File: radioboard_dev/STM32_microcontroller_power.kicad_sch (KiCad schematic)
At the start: 27 parts

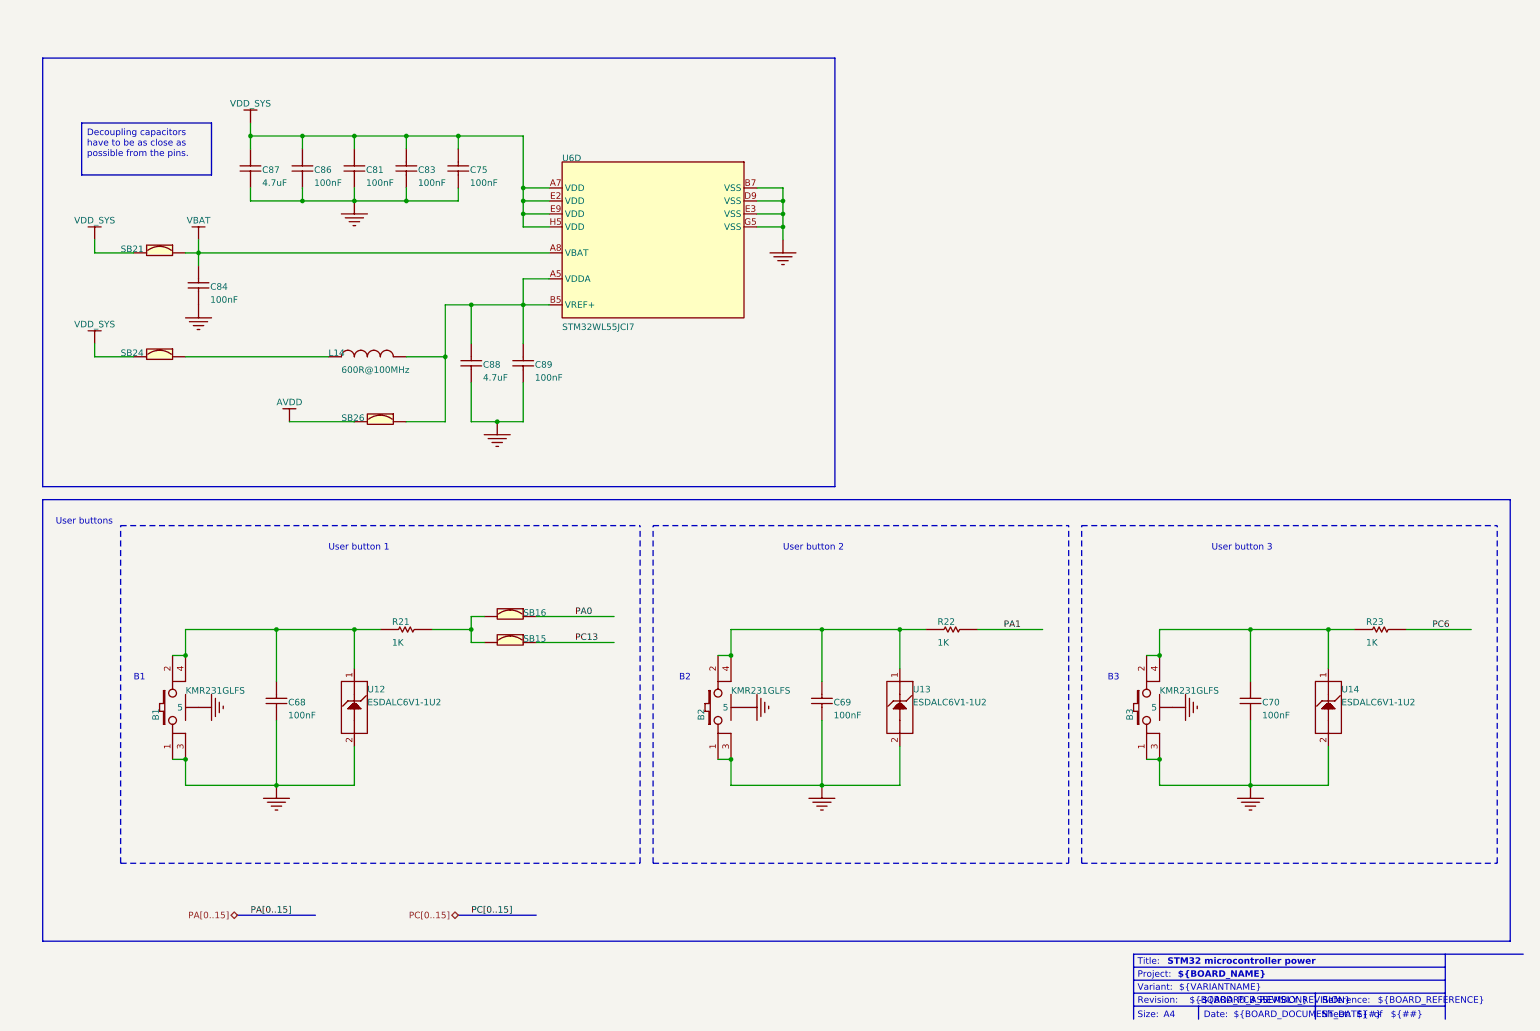
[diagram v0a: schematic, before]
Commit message: added components
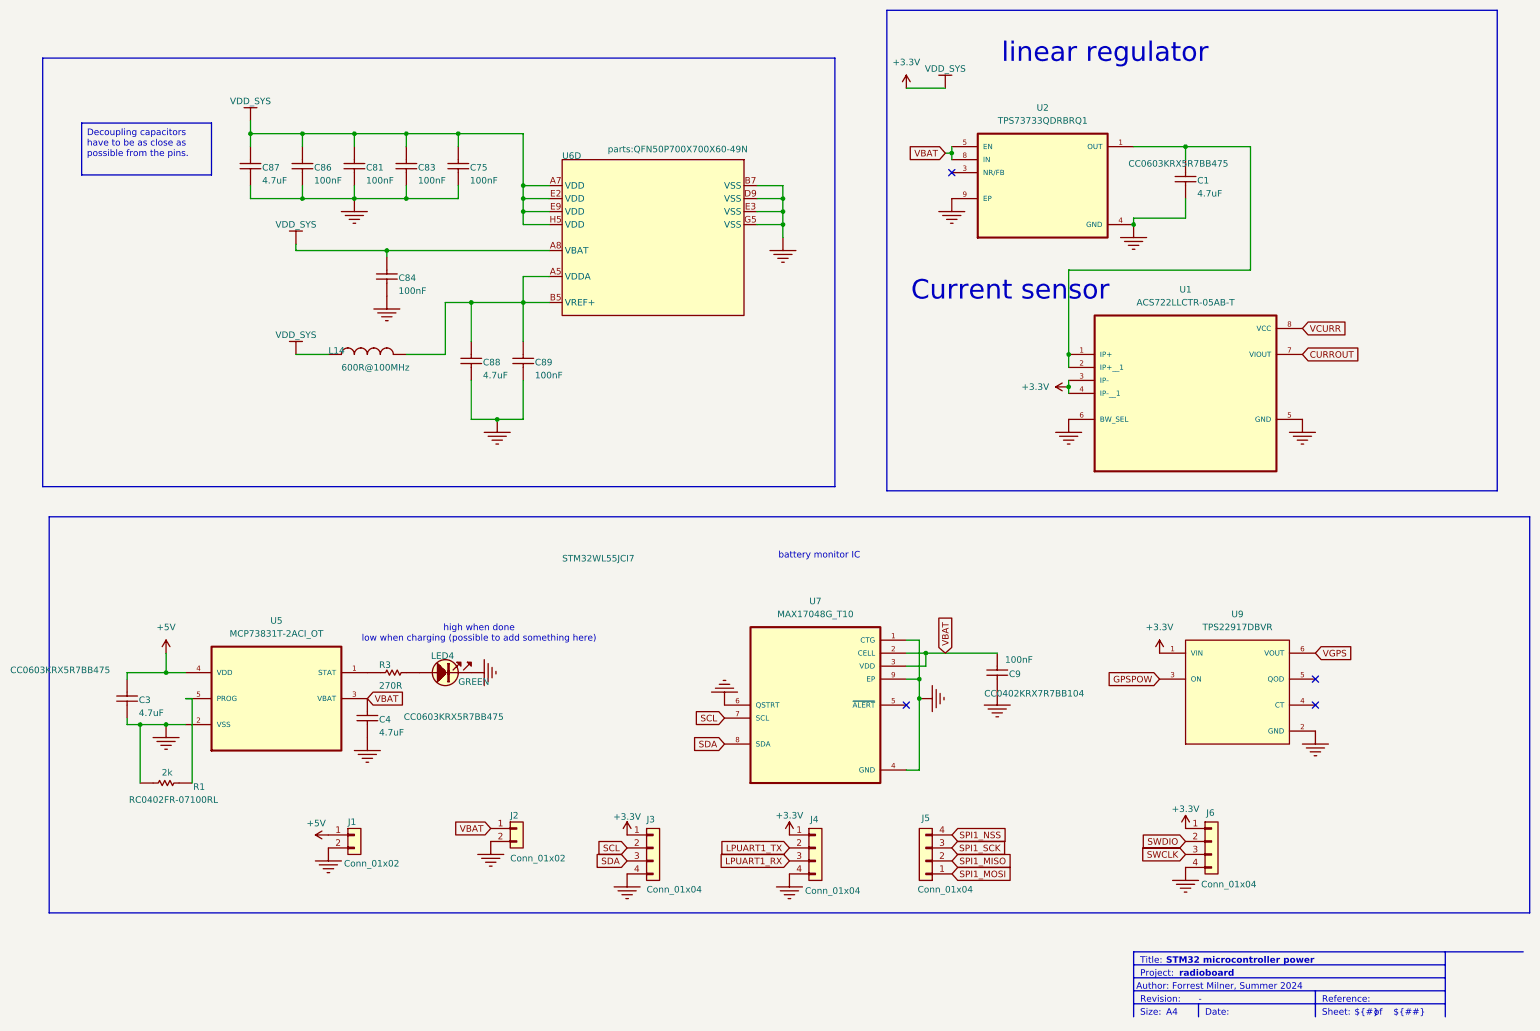
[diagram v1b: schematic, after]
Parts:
- removed B1, B2, B3: (no value), SWI_C&K_Y78B23110FP__ITT_KMR231GLFS, symbol MB1389-altium-import:U_STM32_microcontroller_power_1_SW-PUSH-CMS_KMR2_BLACK
- removed C68, C69, C70: (no value), C0402, symbol MB1389-altium-import:U_STM32_microcontroller_power_1_Capacitor
- removed R21, R22, R23: (no value), R0402, symbol MB1389-altium-import:U_STM32_microcontroller_power_0_Resistor
- removed SB15, SB16, SB21, SB24, SB26: (no value), SOLDER-BRIDGE_R0603-0R, symbol MB1389-altium-import:U_STM32_microcontroller_power_0_SB_ON
- removed U12, U13, U14: (no value), ESD_ST0201, symbol MB1389-altium-import:U_STM32_microcontroller_power_0_ESD-TRANSIL
- added C1, C3, C4: ~, parts:C0603, symbol MB1389-altium-import:U_STM32_microcontroller_RF_1_Capacitor
- added C9: ~, parts:C0402, symbol MB1389-altium-import:U_STM32_microcontroller_RF_3_Capacitor
- added J1, J2: Conn_01x02, Connector_PinHeader_2.54mm:PinHeader_1x01_P2.54mm_Vertical, symbol Connector_Generic:Conn_01x02
- added J3, J4, J5, J6: Conn_01x04, Connector_PinHeader_2.54mm:PinHeader_1x04_P2.54mm_Vertical, symbol Connector_Generic:Conn_01x04
- added LED4: ~, parts:LED_0603_OSRAM_LG-Q396-PS-35_GREEN_1A2K_H0P4, symbol MB1389-altium-import:U_STM32_microcontroller_IOs_0_LED_green_0
- added R1: 2k, parts:R0402, symbol MB1389-altium-import:U_STM32_microcontroller_RF_0_Resistor
- added R3: ~, parts:R0402, symbol MB1389-altium-import:U_STM32_microcontroller_IOs_0_Resistor
- added U1: ACS722LLCTR-05AB-T, ACS722LLCTR-05AB-T:SOIC127P600X175-8N, symbol ACS722LLCTR-05AB-T:ACS722LLCTR-05AB-T
- added U2: TPS73733QDRBRQ1, parts:IC_DRV8601DRBT, symbol TPS73733QDRBRQ1:TPS73733QDRBRQ1
- added U5: MCP73831T-2ACI_OT, parts:SOT95P280X145-5N, symbol MCP73831T-2ACI_OT:MCP73831T-2ACI_OT
- added U7: MAX17048G_T10, MAX17048G_T10:SON50P200X200X80-9N, symbol MAX17048G_T10:MAX17048G_T10
- added U9: TPS22917DBVR, parts:SOT95P280X145-6N, symbol TPS22917DBVR:TPS22917DBVR
- C75, C81, C83, C84, C86, C89: value (none) -> ~; footprint C0402 -> parts:C0402
- C87, C88: value (none) -> ~; footprint C0603 -> parts:C0603
- L14: value (none) -> ~; footprint L0603 -> parts:L0603
- U6: value (none) -> ~; footprint ICC_UFBGA73_5X5_P050 -> parts:QFN50P700X700X60-49N
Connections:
- net VDD_SYS is gone; now on net +3.3V: C75.2, C81.2, C83.2, C86.2, C87.2, U6.A7 (VDD), U6.E2 (VDD), U6.E9 (VDD), U6.H5 (VDD)
- net GND: now also C1.1, C3.1, C4.1, C9.2, J1.2 (Pin_2), J2.2 (Pin_2), J3.4 (Pin_4), J4.4 (Pin_4), J6.4 (Pin_4), LED4.2, R1.2, U1.5 (GND), U1.6 (BW_SEL), U2.4 (GND), U2.9 (EP), U5.2 (VSS), U7.1 (CTG), U7.4 (GND), U7.6 (QSTRT), U7.9 (EP), U9.2 (GND)
- net VBAT: now also C4.2, C9.1, J2.1 (Pin_1), U2.5 (EN), U2.8 (IN), U5.3 (VBAT), U7.2 (CELL), U7.3 (VDD); no longer C84.2, U6.A8 (VBAT)
- net +3.3V: now reaches L14.1
- net +3.3V: now also C84.2, U6.A8 (VBAT), J3.1 (Pin_1), J4.1 (Pin_1), J6.1 (Pin_1), U1.3 (IP-), U1.4 (IP-__1), U9.1 (VIN)
- new net: R3.1, U5.1 (STAT)
- new net: LED4.1, R3.2
- new net: C1.2, U1.1 (IP+), U1.2 (IP+__1), U2.1 (OUT)
- new net: R1.1, U5.5 (PROG)
- new net +5V: C3.2, J1.1 (Pin_1), U5.4 (VDD)
- new net CURROUT: U1.7 (VIOUT)
- new net GPSPOW: U9.3 (ON)
- new net LPUART1_RX: J4.3 (Pin_3)
- new net LPUART1_TX: J4.2 (Pin_2)
- new net SCL: J3.2 (Pin_2), U7.7 (SCL)
- new net SDA: J3.3 (Pin_3), U7.8 (SDA)
- new net SPI1_SCK: J5.3 (Pin_3)
- new net SWCLK: J6.3 (Pin_3)
- new net SWDIO: J6.2 (Pin_2)
- new net VCURR: U1.8 (VCC)
- new net VGPS: U9.6 (VOUT)
- no-connect marks 0 -> 4
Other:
- note added: "Author: Forrest Milner, Summer 2024"
- note added: "Current sensor"
- note added: "battery monitor IC"
- note added: "high when done low when charging (possible to add something here)"
- note added: "linear regulator"
- note added: "radioboard"
- note removed: "${BOARD_ASSEMBLY_REVISION}"
- note removed: "${BOARD_DOCUMENT_DATE}"
- note removed: "${BOARD_NAME}"
- note removed: "${BOARD_PCB_REVISION}"
- note removed: "${BOARD_REFERENCE}"
- note removed: "${VARIANTNAME}"
- note removed: "B1"
- note removed: "B2"
- note removed: "B3"
- note removed: "User button 1"
- note removed: "User button 2"
- note removed: "User button 3"
- note removed: "User buttons"
- note removed: "Variant:"
- moved on the sheet: C84

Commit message: finish schematic and clear pcb
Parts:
- removed C75, C81, C83, C84, C86, C89: ~, parts:C0402, symbol MB1389-altium-import:U_STM32_microcontroller_power_1_Capacitor
- removed C87, C88: ~, parts:C0603, symbol MB1389-altium-import:U_STM32_microcontroller_power_1_Capacitor
- removed L14: ~, parts:L0603, symbol MB1389-altium-import:U_STM32_microcontroller_power_0_BEAD
- removed U6: ~, parts:QFN50P700X700X60-49N, symbol MB1389-altium-import:U_STM32_microcontroller_power_0_STM32WL5x_BGA73
- J1, J2: footprint Connector_PinHeader_2.54mm:PinHeader_1x01_P2.54mm_Vertical -> Connector_PinHeader_2.54mm:PinHeader_1x02_P2.54mm_Vertical
- U7: footprint MAX17048G_T10:SON50P200X200X80-9N -> parts:SON50P200X200X80-9N
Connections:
- net SPI1_MISO: now also J5.2 (Pin_2)
- net SPI1_MOSI: now also J5.1 (Pin_1)
- net SPI1_NSS: now also J5.4 (Pin_4)
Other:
- moved on the sheet: J5

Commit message: footprints
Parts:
- U1: footprint ACS722LLCTR-05AB-T:SOIC127P600X175-8N -> parts:SOIC127P600X175-8N
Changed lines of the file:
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@@
 		)
 	)
+	(wire
+		(pts
+			(xy 179.07 49.53) (xy 180.34 49.53)
+		)
+		(stroke
+			(width 0)
+			(type default)
+		)
+	)
 	(polyline
 		(pts
@@
 	(wire
 		(pts
+			(xy 179.07 52.07) (xy 179.07 49.53)
+		)
+		(stroke
+			(width 0)
+			(type default)
+		)
+	)
+	(wire
+		(pts
 			(xy 19.05 142.24) (xy 19.05 143.51)
 		)
@@
 	(symbol
 		(lib_id "MB1389-altium-import:GND_POWER_GROUND")
-		(at 180.34 49.53 0)
+		(at 179.07 52.07 0)
 		(unit 1)
 		(exclude_from_sim no)
@@
 		(dnp no)
 		(property "Reference" "#PWR05"
-			(at 180.34 49.53 0)
+			(at 179.07 52.07 0)
 			(effects
 				(font
@@
 		)
 		(property "Value" "GND"
-			(at 180.34 55.88 0)
+			(at 179.07 58.42 0)
 			(effects
 				(font
@@
 		)
 		(property "Footprint" ""
-			(at 180.34 49.53 0)
+			(at 179.07 52.07 0)
 			(effects
 				(font
@@
 		)
 		(property "Datasheet" ""
-			(at 180.34 49.53 0)
+			(at 179.07 52.07 0)
 			(effects
 				(font
@@
 		)
 		(property "Description" ""
-			(at 180.34 49.53 0)
+			(at 179.07 52.07 0)
 			(effects
 				(font
@@
 				)
 				(justify left)
+				(hide yes)
 			)
 		)
@@
 				)
 				(justify left)
+				(hide yes)
 			)
 		)
@@
 			)
 		)
-		(property "Footprint" "ACS722LLCTR-05AB-T:SOIC127P600X175-8N"
+		(property "Footprint" "parts:SOIC127P600X175-8N"
 			(at 226.06 85.09 0)
 			(effects
@@
 				)
 				(justify left)
+				(hide yes)
 			)
 		)
@@
 					(size 1.27 1.27)
 				)
+				(hide yes)
 			)
 		)

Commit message: added gps
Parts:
- removed U9: TPS22917DBVR, parts:SOT95P280X145-6N, symbol TPS22917DBVR:TPS22917DBVR
- renumbered J3 to J9, U7 to U11, U2 to U12, U1 to U13
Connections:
- no-connect marks 4 -> 2

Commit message: all footprints done
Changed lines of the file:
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@@
 	)
 	(no_connect
-		(at 171.45 148.59)
+		(at 171.45 149.86)
 	)
 	(wire
@@
 		)
 	)
+	(wire
+		(pts
+			(xy 173.99 135.89) (xy 173.99 143.51)
+		)
+		(stroke
+			(width 0)
+			(type default)
+		)
+	)
 	(polyline
 		(pts
@@
 	(wire
 		(pts
-			(xy 173.99 143.51) (xy 173.99 147.32)
-		)
-		(stroke
-			(width 0)
-			(type default)
-		)
-	)
-	(wire
-		(pts
 			(xy 173.99 147.32) (xy 173.99 161.29)
 		)
@@
 	(wire
 		(pts
+			(xy 173.99 143.51) (xy 173.99 147.32)
+		)
+		(stroke
+			(width 0)
+			(type default)
+		)
+	)
+	(wire
+		(pts
 			(xy 215.9 53.34) (xy 215.9 54.61)
 		)
@@
 		)
 	)
+	(wire
+		(pts
+			(xy 171.45 149.86) (xy 171.45 148.59)
+		)
+		(stroke
+			(width 0)
+			(type default)
+		)
+	)
 	(polyline
 		(pts
@@
 		)
 	)
-	(wire
-		(pts
-			(xy 173.99 135.89) (xy 173.99 143.51)
-		)
-		(stroke
-			(width 0)
-			(type default)
-		)
-	)
 	(rectangle
 		(start 3.81 111.76)
@@
 		(pin "7"
 		)
+		(instances
+			(project ""
+				(path "/d463a497-8f2e-444e-8cd9-7512b15bd4f7/1ca16541-0f9c-45cc-84d4-3e816fa9d744"
+					(reference "U11")
+					(unit 1)
+				)
+			)
+		)
 	)
 	(symbol
@@
 		(pin "8"
 		)
+		(instances
+			(project ""
+				(path "/d463a497-8f2e-444e-8cd9-7512b15bd4f7/1ca16541-0f9c-45cc-84d4-3e816fa9d744"
+					(reference "U12")
+					(unit 1)
+				)
+			)
+		)
 	)

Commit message: roughly placed
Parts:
- added BT1: BH-18650-PC, parts:BAT_BH-18650-PC, symbol BH-18650-PC:BH-18650-PC
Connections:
- net GND: now also BT1.N
- net VBAT: now also BT1.P
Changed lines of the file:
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@@
 		)
 	)
+	(global_label "VBAT"
+		(shape input)
+		(at 82.55 55.88 90)
+		(fields_autoplaced yes)
+		(effects
+			(font
+				(size 1.27 1.27)
+			)
+			(justify left)
+		)
+		(property "Intersheetrefs" "${INTERSHEET_REFS}"
+			(at 82.55 48.48 90)
+			(effects
+				(font
+					(size 1.27 1.27)
+				)
+				(justify left)
+				(hide yes)
+			)
+		)
+	)
 	(global_label "SPI1_MOSI"
 		(shape input)
@@
 	)
 	(symbol
+		(lib_id "MB1389-altium-import:GND_POWER_GROUND")
+		(at 82.55 68.58 0)
+		(unit 1)
+		(exclude_from_sim no)
+		(in_bom yes)
+		(on_board yes)
+		(dnp no)
+		(property "Reference" "#PWR046"
+			(at 82.55 68.58 0)
+			(effects
+				(font
+					(size 1.27 1.27)
+				)
+				(hide yes)
+			)
+		)
+		(property "Value" "GND"
+			(at 82.55 74.93 0)
+			(effects
+				(font
+					(size 1.27 1.27)
+				)
+				(hide yes)
+			)
+		)
+		(property "Footprint" ""
+			(at 82.55 68.58 0)
+			(effects
+				(font
+					(size 1.27 1.27)
+				)
+				(hide yes)
+			)
+		)
+		(property "Datasheet" ""
+			(at 82.55 68.58 0)
+			(effects
+				(font
+					(size 1.27 1.27)
+				)
+				(hide yes)
+			)
+		)
+		(property "Description" ""
+			(at 82.55 68.58 0)
+			(effects
+				(font
+					(size 1.27 1.27)
+				)
+				(hide yes)
+			)
+		)
+		(pin ""
+		)
+		(instances
+			(project "radioboard_dev"
+				(path "/d463a497-8f2e-444e-8cd9-7512b15bd4f7/1ca16541-0f9c-45cc-84d4-3e816fa9d744"
+					(reference "#PWR046")
+					(unit 1)
+				)
+			)
+		)
+	)
+	(symbol
 		(lib_id "power:+3.3V")
 		(at 171.45 27.94 0)
@@
 					(unit 1)
 				)
+			)
+		)
+	)
+	(symbol
+		(lib_id "BH-18650-PC:BH-18650-PC")
+		(at 82.55 63.5 270)
+		(unit 1)
+		(exclude_from_sim no)
+		(in_bom yes)
+		(on_board yes)
+		(dnp no)
+		(fields_autoplaced yes)
+		(property "Reference" "BT1"
+			(at 86.36 59.6899 90)
+			(effects
+				(font
+					(size 1.27 1.27)
+				)
+				(justify left)
+			)
+		)
+		(property "Value" "BH-18650-PC"
+			(at 86.36 62.2299 90)
+			(effects
+				(font
+					(size 1.27 1.27)
+				)
+				(justify left)
+			)
+		)
+		(property "Footprint" "parts:BAT_BH-18650-PC"
+			(at 82.55 63.5 0)
+			(effects
+				(font
+					(size 1.27 1.27)
+				)
+				(justify bottom)
+				(hide yes)
+			)
+		)
+		(property "Datasheet" ""
+			(at 82.55 63.5 0)
+			(effects
+				(font
+					(size 1.27 1.27)
+				)
+				(hide yes)
+			)
+		)
+		(property "Description" ""
+			(at 82.55 63.5 0)
+			(effects
+				(font
+					(size 1.27 1.27)
+				)
+				(hide yes)
+			)
+		)
+		(property "PARTREV" "05/17/19"
+			(at 82.55 63.5 0)
+			(effects
+				(font
+					(size 1.27 1.27)
+				)
+				(justify bottom)
+				(hide yes)
+			)
+		)
+		(property "STANDARD" "Manufacturer Recommendation"
+			(at 82.55 63.5 0)
+			(effects
+				(font
+					(size 1.27 1.27)
+				)
+				(justify bottom)
+				(hide yes)
+			)
+		)
+		(property "MAXIMUM_PACKAGE_HEIGHT" "21.31mm"
+			(at 82.55 63.5 0)
+			(effects
+				(font
+					(size 1.27 1.27)
+				)
+				(justify bottom)
+				(hide yes)
+			)
+		)
+		(property "MANUFACTURER" "MPD"
+			(at 82.55 63.5 0)
+			(effects
+				(font
+					(size 1.27 1.27)
+				)
+				(justify bottom)
+				(hide yes)
+			)
+		)
+		(pin "N"
+		)
+		(pin "P"
+		)
+		(instances
+			(project ""
+				(path "/d463a497-8f2e-444e-8cd9-7512b15bd4f7/1ca16541-0f9c-45cc-84d4-3e816fa9d744"
+					(reference "BT1")
+					(unit 1)
+				)

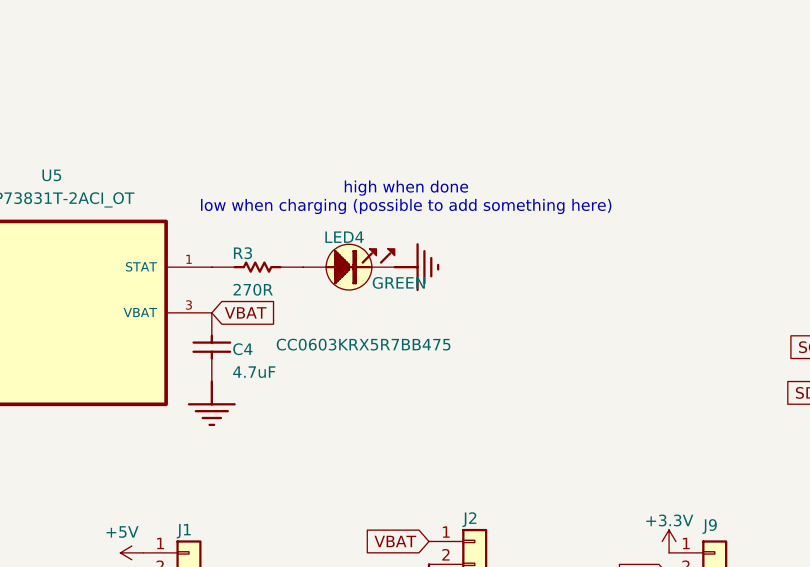
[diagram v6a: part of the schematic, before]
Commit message: bom changes
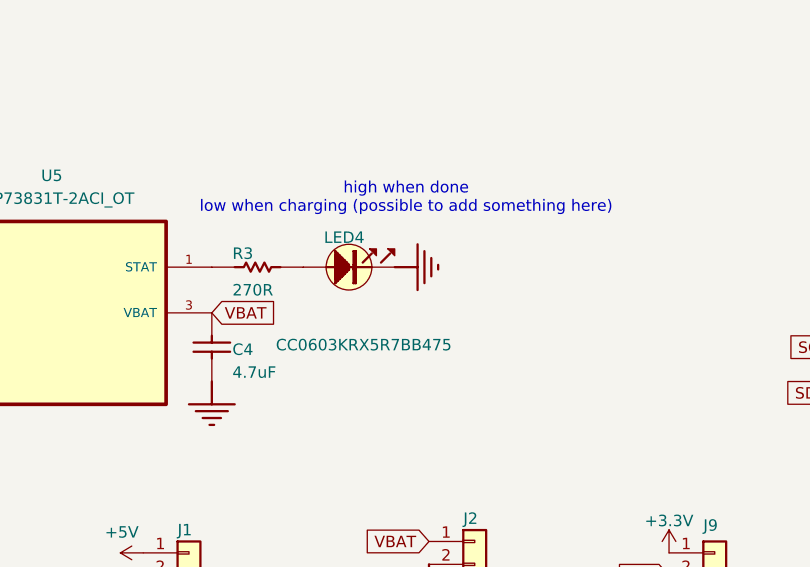
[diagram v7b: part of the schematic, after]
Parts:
- BT1: MANUFACTURER MPD -> (none); MAXIMUM_PACKAGE_HEIGHT 21.31mm -> (none); PARTREV 05/17/19 -> (none); STANDARD Manufacturer Recommendation -> (none)
- LED4: footprint parts:LED_0603_OSRAM_LG-Q396-PS-35_GREEN_1A2K_H0P4 -> LED_0603_OSRAM_LG-Q396-PS-35_GREEN_1A2K_H0P4; ALTERNATE_MANUFACTURER VISHAY SEMICONDUCTOR OPTO DIVISION -> (none); ALTERNATE_MANUFACTURER_PART_NUMBER VLMTG1300-GS08 -> (none); ALTIUM_VALUE GREEN -> (none); COMPONENTLINK1DESCRIPTION Datasheet -> (none); COMPONENTLINK1URL http://tunmcdsvn.tun.st.com/Component_Datasheet_Library/Tru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 -> (none); ECCN_EU n/a -> (none); ECCN_US n/a -> (none); INTERNAL_PART_NUMBER MCD-00588 -> (none); MANUFACTURER OSRAM OPTO SEMICONDUCTORS -> (none); MANUFACTURER_PART_NUMBER LG Q396-PS-35 -> (none); ORDER_CODE_DIGIKEY LG Q396-PS-35-ND -> (none); PACKAGE LED 0603 -> (none); PART_TYPE Display -> (none); PROVIDED_BY SUBCO -> (none); STATUS Released -> (none)
- U11: Check_prices https://www.snapeda.com/parts/MAX17048G+T10/Analog+Devices/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 -> (none); Description_1 3µA 1-Cell/2-Cell Fuel Gauge with ModelGauge -> (none); DigiKey_Part_Number MAX17048G+T10TR-ND -> (none); MF Analog Devices -> (none); MP MAX17048G+T10 -> (none); Package TDFN-8 Maxim -> (none); Purchase-URL https://www.snapeda.com/api/url_track_click_mouser/?unipart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 -> (none); SnapEDA_Link https://www.snapeda.com/parts/MAX17048G+T10/Analog+Devices/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 -> (none)
- U12: Check_prices https://www.snapeda.com/parts/TPS73733QDRBRQ1/Texas+Instrum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 -> (none); Description_1 Automotive 1-A, ultra-low-dropout voltage regulator with re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 -> (none); DigiKey_Part_Number 296-24157-2-ND -> (none); MF Texas Instruments -> (none); MP TPS73733QDRBRQ1 -> (none); Package VSON-8 Texas Instruments -> (none); Purchase-URL https://www.snapeda.com/api/url_track_click_mouser/?unipart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 -> (none); SnapEDA_Link https://www.snapeda.com/parts/TPS73733QDRBRQ1/Texas+Instrum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 -> (none)
- U13: Manufacturer Allegro MicroSystems LLC -> (none); Package SOIC127P600X175-8N -> (none)
- U5: Check_prices https://www.snapeda.com/parts/MCP73831T-2ACI/OT/Microchip/v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 -> (none); Description_1 TINY INTEGRATED LI-ION/LI-POLY CHARGE MGNT CONTROLLER, 4.2V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 -> (none); DigiKey_Part_Number MCP73831T-2ACI/OTTR-ND -> (none); MF Microchip -> (none); MP MCP73831T-2ACI/OT -> (none); MPN MCP73831T-2ACI/OT -> (none); OC_FARNELL 1332158 -> (none); OC_NEWARK 56K7045 -> (none); PACKAGE SOT-5 -> (none); Package SOT-23 Microchip -> (none); Purchase-URL https://www.snapeda.com/api/url_track_click_mouser/?unipart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 -> (none); SUPPLIER Microchip -> (none); SnapEDA_Link https://www.snapeda.com/parts/MCP73831T-2ACI/OT/Microchip/v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 -> (none)
